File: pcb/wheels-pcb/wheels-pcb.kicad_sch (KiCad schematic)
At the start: 16 parts, among them J1 Motor_1, J2 Motor_2, J3 Motor_3, J4 Motor_4, J5 Conn_01x03, U1 L293D, U2 L293D, U3 ESP32S_38P

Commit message: pcb-modification
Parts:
- J1, J2, J3, J4: footprint Connectors_JST:JST_EH_B06B-EH-A_06x2.50mm_Straight -> Connector_JST:JST_EH_B6B-EH-A_1x06_P2.50mm_Vertical
- J5: footprint Connectors_JST:JST_EH_S03B-EH_03x2.50mm_Angled -> Connector_JST:JST_EH_S3B-EH_1x03_P2.50mm_Horizontal
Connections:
- net at U3.27 (GPIO16): now also U2.9 (EN3,4)
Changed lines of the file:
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@@
 (kicad_sch
-	(version 20231120)
+	(version 20250114)
 	(generator "eeschema")
-	(generator_version "8.0")
+	(generator_version "9.0")
 	(paper "A4")
+	(text "+12v\n"
+		(exclude_from_sim no)
+		(at 148.971 125.603 0)
+		(effects
+			(font
+				(size 0.762 0.762)
+			)
+		)
+	)
+	(text "GND"
+		(exclude_from_sim no)
+		(at 155.829 125.603 0)
+		(effects
+			(font
+				(size 0.762 0.762)
+			)
+		)
+	)
+	(text "+5v\n"
+		(exclude_from_sim no)
+		(at 152.527 125.603 0)
+		(effects
+			(font
+				(size 0.762 0.762)
+			)
+		)
+	)
 	(junction
 		(at 83.82 69.85)
@@
 	(wire
 		(pts
+			(xy 191.77 107.95) (xy 196.85 107.95)
+		)
+		(stroke
+			(width 0)
+			(type default)
+		)
+	)
+	(wire
+		(pts
 			(xy 33.02 127) (xy 123.19 127)
 		)
@@
 	(wire
 		(pts
+			(xy 166.37 100.33) (xy 191.77 100.33)
+		)
+		(stroke
+			(width 0)
+			(type default)
+		)
+	)
+	(wire
+		(pts
 			(xy 76.2 102.87) (xy 49.53 102.87)
 		)
@@
 	(wire
 		(pts
+			(xy 191.77 100.33) (xy 191.77 107.95)
+		)
+		(stroke
+			(width 0)
+			(type default)
+		)
+	)
+	(wire
+		(pts
 			(xy 245.11 125.73) (xy 245.11 119.38)
 		)
@@
 		)
 	)
-	(text "+12v\n"
-		(exclude_from_sim no)
-		(at 148.971 125.603 0)
-		(effects
-			(font
-				(size 0.762 0.762)
-			)
-		)
-	)
-	(text "GND"
-		(exclude_from_sim no)
-		(at 155.829 125.603 0)
-		(effects
-			(font
-				(size 0.762 0.762)
-			)
-		)
-	)
-	(text "+5v\n"
-		(exclude_from_sim no)
-		(at 152.527 125.603 0)
-		(effects
-			(font
-				(size 0.762 0.762)
-			)
-		)
-	)
 	(symbol
 		(lib_id "Diode:1N4001")
@@
 			)
 		)
-		(property "Footprint" "Connectors_JST:JST_EH_S03B-EH_03x2.50mm_Angled"
+		(property "Footprint" "Connector_JST:JST_EH_S3B-EH_1x03_P2.50mm_Horizontal"
 			(at 152.4 128.27 0)
 			(effects
@@
 			)
 		)
-		(property "Footprint" "Connectors_JST:JST_EH_B06B-EH-A_06x2.50mm_Straight"
+		(property "Footprint" "Connector_JST:JST_EH_B6B-EH-A_1x06_P2.50mm_Vertical"
 			(at 27.94 129.54 0)
 			(effects
@@
 			)
 		)
-		(property "Footprint" "Connectors_JST:JST_EH_B06B-EH-A_06x2.50mm_Straight"
+		(property "Footprint" "Connector_JST:JST_EH_B6B-EH-A_1x06_P2.50mm_Vertical"
 			(at 27.94 73.66 0)
 			(effects
@@
 			)
 		)
-		(property "Footprint" "Connectors_JST:JST_EH_B06B-EH-A_06x2.50mm_Straight"
+		(property "Footprint" "Connector_JST:JST_EH_B6B-EH-A_1x06_P2.50mm_Vertical"
 			(at 270.51 119.38 0)
 			(effects
@@
 			)
 		)
-		(property "Footprint" "Connectors_JST:JST_EH_B06B-EH-A_06x2.50mm_Straight"
+		(property "Footprint" "Connector_JST:JST_EH_B6B-EH-A_1x06_P2.50mm_Vertical"
 			(at 270.51 60.96 0)
 			(effects
@@
 		(on_board yes)
 		(dnp no)
-		(fields_autoplaced yes)
 		(property "Reference" "U2"
 			(at 214.2841 69.85 0)
@@
 		)
 	)
+	(embedded_fonts no)
 )

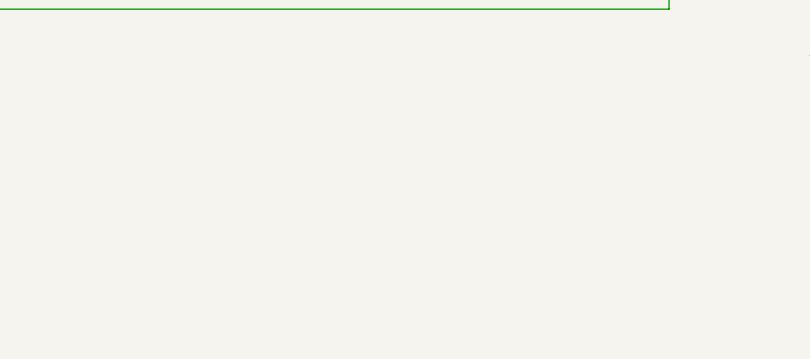
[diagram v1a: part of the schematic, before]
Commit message: direct kinematiks addition
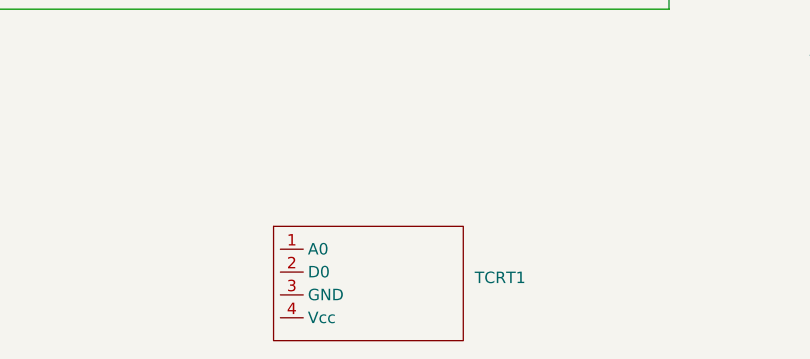
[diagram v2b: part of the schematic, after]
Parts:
- added TCRT1: ~, TCRT5000:TCRT5000, symbol TCRT5000:TCRT5000
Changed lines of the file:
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@@
+	)
+	(symbol
+		(lib_id "TCRT5000:TCRT5000")
+		(at 80.01 153.67 0)
+		(unit 1)
+		(exclude_from_sim no)
+		(in_bom yes)
+		(on_board yes)
+		(dnp no)
+		(fields_autoplaced yes)
+		(property "Reference" "TCRT1"
+			(at 104.14 159.3849 0)
+			(effects
+				(font
+					(size 1.27 1.27)
+				)
+				(justify left)
+			)
+		)
+		(property "Value" "~"
+			(at 104.14 161.29 0)
+			(effects
+				(font
+					(size 1.27 1.27)
+				)
+				(justify left)
+			)
+		)
+		(property "Footprint" "TCRT5000:TCRT5000"
+			(at 80.01 153.67 0)
+			(effects
+				(font
+					(size 1.27 1.27)
+				)
+				(hide yes)
+			)
+		)
+		(property "Datasheet" ""
+			(at 80.01 153.67 0)
+			(effects
+				(font
+					(size 1.27 1.27)
+				)
+				(hide yes)
+			)
+		)
+		(property "Description" ""
+			(at 80.01 153.67 0)
+			(effects
+				(font
+					(size 1.27 1.27)
+				)
+				(hide yes)
+			)
+		)
+		(pin "1"
+		)
+		(pin "2"
+		)
+		(pin "4"
+		)
+		(pin "3"
+		)
+		(instances
+			(project ""
+				(path "/1ed4948a-430c-468a-a4d9-08bf97f1a7c3"
+					(reference "TCRT1")
+					(unit 1)
+				)
+			)
+		)
 	)
 	(symbol

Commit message: direct kinematics addition
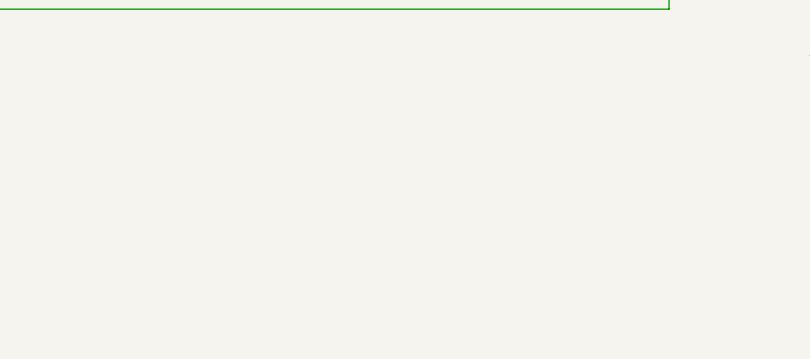
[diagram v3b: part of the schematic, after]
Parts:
- removed TCRT1: ~, TCRT5000:TCRT5000, symbol TCRT5000:TCRT5000
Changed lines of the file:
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@@
-	)
-	(symbol
-		(lib_id "TCRT5000:TCRT5000")
-		(at 80.01 153.67 0)
-		(unit 1)
-		(exclude_from_sim no)
-		(in_bom yes)
-		(on_board yes)
-		(dnp no)
-		(fields_autoplaced yes)
-		(property "Reference" "TCRT1"
-			(at 104.14 159.3849 0)
-			(effects
-				(font
-					(size 1.27 1.27)
-				)
-				(justify left)
-			)
-		)
-		(property "Value" "~"
-			(at 104.14 161.29 0)
-			(effects
-				(font
-					(size 1.27 1.27)
-				)
-				(justify left)
-			)
-		)
-		(property "Footprint" "TCRT5000:TCRT5000"
-			(at 80.01 153.67 0)
-			(effects
-				(font
-					(size 1.27 1.27)
-				)
-				(hide yes)
-			)
-		)
-		(property "Datasheet" ""
-			(at 80.01 153.67 0)
-			(effects
-				(font
-					(size 1.27 1.27)
-				)
-				(hide yes)
-			)
-		)
-		(property "Description" ""
-			(at 80.01 153.67 0)
-			(effects
-				(font
-					(size 1.27 1.27)
-				)
-				(hide yes)
-			)
-		)
-		(pin "1"
-		)
-		(pin "2"
-		)
-		(pin "4"
-		)
-		(pin "3"
-		)
-		(instances
-			(project ""
-				(path "/1ed4948a-430c-468a-a4d9-08bf97f1a7c3"
-					(reference "TCRT1")
-					(unit 1)
-				)
-			)
-		)
 	)
 	(symbol

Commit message: pcb correction
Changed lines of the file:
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@@
-	)
-	(junction
-		(at 222.25 82.55)
-		(diameter 0)
-		(color 0 0 0 0)
 	)
 	(junction
@@
 	)
 	(junction
-		(at 222.25 97.79)
-		(diameter 0)
-		(color 0 0 0 0)
-	)
-	(junction
-		(at 76.2 107.95)
-		(diameter 0)
-		(color 0 0 0 0)
-	)
-	(junction
 		(at 86.36 69.85)
 		(diameter 0)
@@
 	)
 	(junction
-		(at 222.25 102.87)
-		(diameter 0)
-		(color 0 0 0 0)
-	)
-	(junction
-		(at 76.2 92.71)
-		(diameter 0)
-		(color 0 0 0 0)
-	)
-	(junction
 		(at 238.76 95.25)
-		(diameter 0)
-		(color 0 0 0 0)
-	)
-	(junction
-		(at 222.25 87.63)
-		(diameter 0)
-		(color 0 0 0 0)
-	)
-	(junction
-		(at 76.2 102.87)
 		(diameter 0)
 		(color 0 0 0 0)
@@
 	)
 	(junction
-		(at 76.2 87.63)
-		(diameter 0)
-		(color 0 0 0 0)
-	)
-	(junction
 		(at 204.47 120.65)
 		(diameter 0)
@@
 	(wire
 		(pts
-			(xy 78.74 87.63) (xy 76.2 87.63)
-		)
-		(stroke
-			(width 0)
-			(type default)
-		)
-	)
-	(wire
-		(pts
 			(xy 212.09 118.11) (xy 212.09 120.65)
 		)
@@
 	(wire
 		(pts
-			(xy 78.74 107.95) (xy 76.2 107.95)
-		)
-		(stroke
-			(width 0)
-			(type default)
-		)
-	)
-	(wire
-		(pts
 			(xy 248.92 97.79) (xy 265.43 97.79)
 		)
@@
 	(wire
 		(pts
-			(xy 78.74 92.71) (xy 76.2 92.71)
-		)
-		(stroke
-			(width 0)
-			(type default)
-		)
-	)
-	(wire
-		(pts
 			(xy 247.65 106.68) (xy 248.92 106.68)
 		)
@@
 	(wire
 		(pts
-			(xy 219.71 102.87) (xy 222.25 102.87)
-		)
-		(stroke
-			(width 0)
-			(type default)
-		)
-	)
-	(wire
-		(pts
 			(xy 173.99 60.96) (xy 173.99 77.47)
 		)
@@
 	(wire
 		(pts
-			(xy 219.71 82.55) (xy 222.25 82.55)
-		)
-		(stroke
-			(width 0)
-			(type default)
-		)
-	)
-	(wire
-		(pts
 			(xy 182.88 125.73) (xy 245.11 125.73)
 		)
@@
 	(wire
 		(pts
-			(xy 219.71 97.79) (xy 222.25 97.79)
-		)
-		(stroke
-			(width 0)
-			(type default)
-		)
-	)
-	(wire
-		(pts
 			(xy 196.85 97.79) (xy 196.85 95.25)
 		)
@@
 	(wire
 		(pts
-			(xy 219.71 87.63) (xy 222.25 87.63)
-		)
-		(stroke
-			(width 0)
-			(type default)
-		)
-	)
-	(wire
-		(pts
 			(xy 195.58 97.79) (xy 166.37 97.79)
 		)
@@
 		)
 		(stroke
-			(width 0)
-			(type default)
-		)
-	)
-	(wire
-		(pts
-			(xy 78.74 102.87) (xy 76.2 102.87)
-		)
-		(stroke

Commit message: blueprints addition
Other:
- company: (none) -> Manuel Piña Olivas
- title: (none) -> Wheels PCB
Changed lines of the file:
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@@
 	(generator_version "9.0")
 	(paper "A4")
+	(title_block
+		(title "Wheels PCB")
+		(date "2025-04-01")
+		(rev "1.0.0")
+		(company "Manuel Piña Olivas")
+	)
 	(text "+12v\n"
 		(exclude_from_sim no)

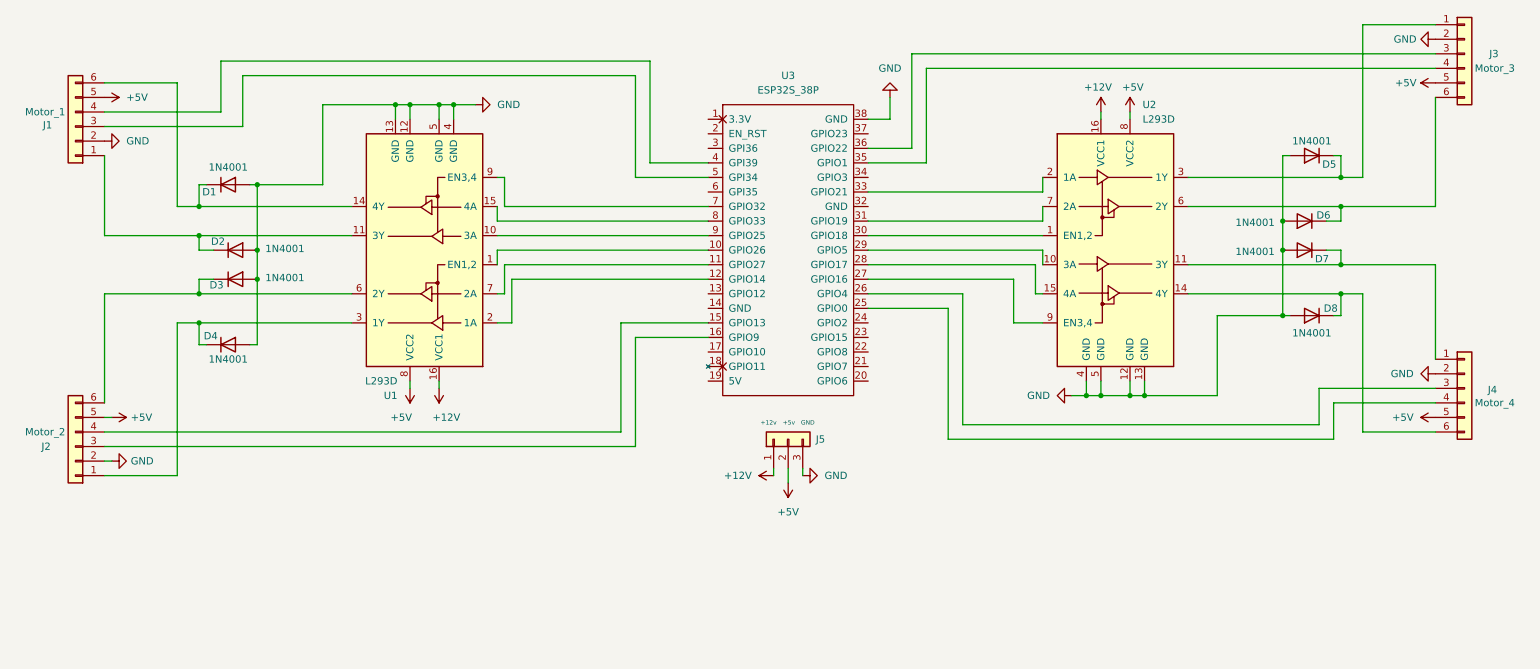
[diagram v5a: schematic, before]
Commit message: Canged Micro ROS code and PCB design also
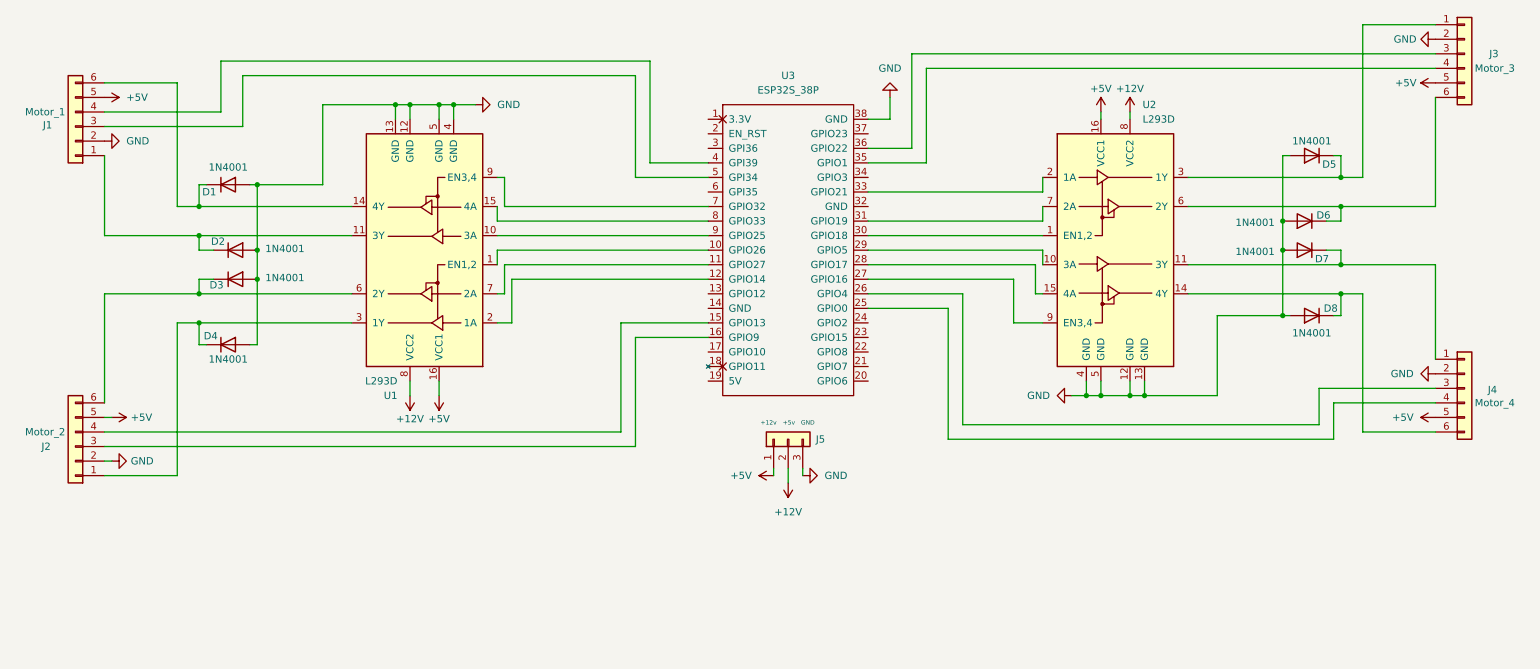
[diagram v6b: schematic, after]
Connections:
- net +12V: now also J5.2 (Pin_2), U1.8 (VCC2), U2.8 (VCC2); no longer J5.1 (Pin_1), U1.16 (VCC1), U2.16 (VCC1)
- net +5V: now also J5.1 (Pin_1), U1.16 (VCC1), U2.16 (VCC1); no longer J5.2 (Pin_2), U1.8 (VCC2), U2.8 (VCC2)
